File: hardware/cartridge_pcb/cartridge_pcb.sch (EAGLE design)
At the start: 88 parts, among them IC1 LM1117MPX-ADJ, Q1 2N7002, Q2 2N7002, Q3 2N7002, Q4 2N7002, Q5 2N7002, U1 MCP23017-E/SO, U2 ADS1015IDGST, U3 MCP23017-E/SO, U4 TXB0108PWR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

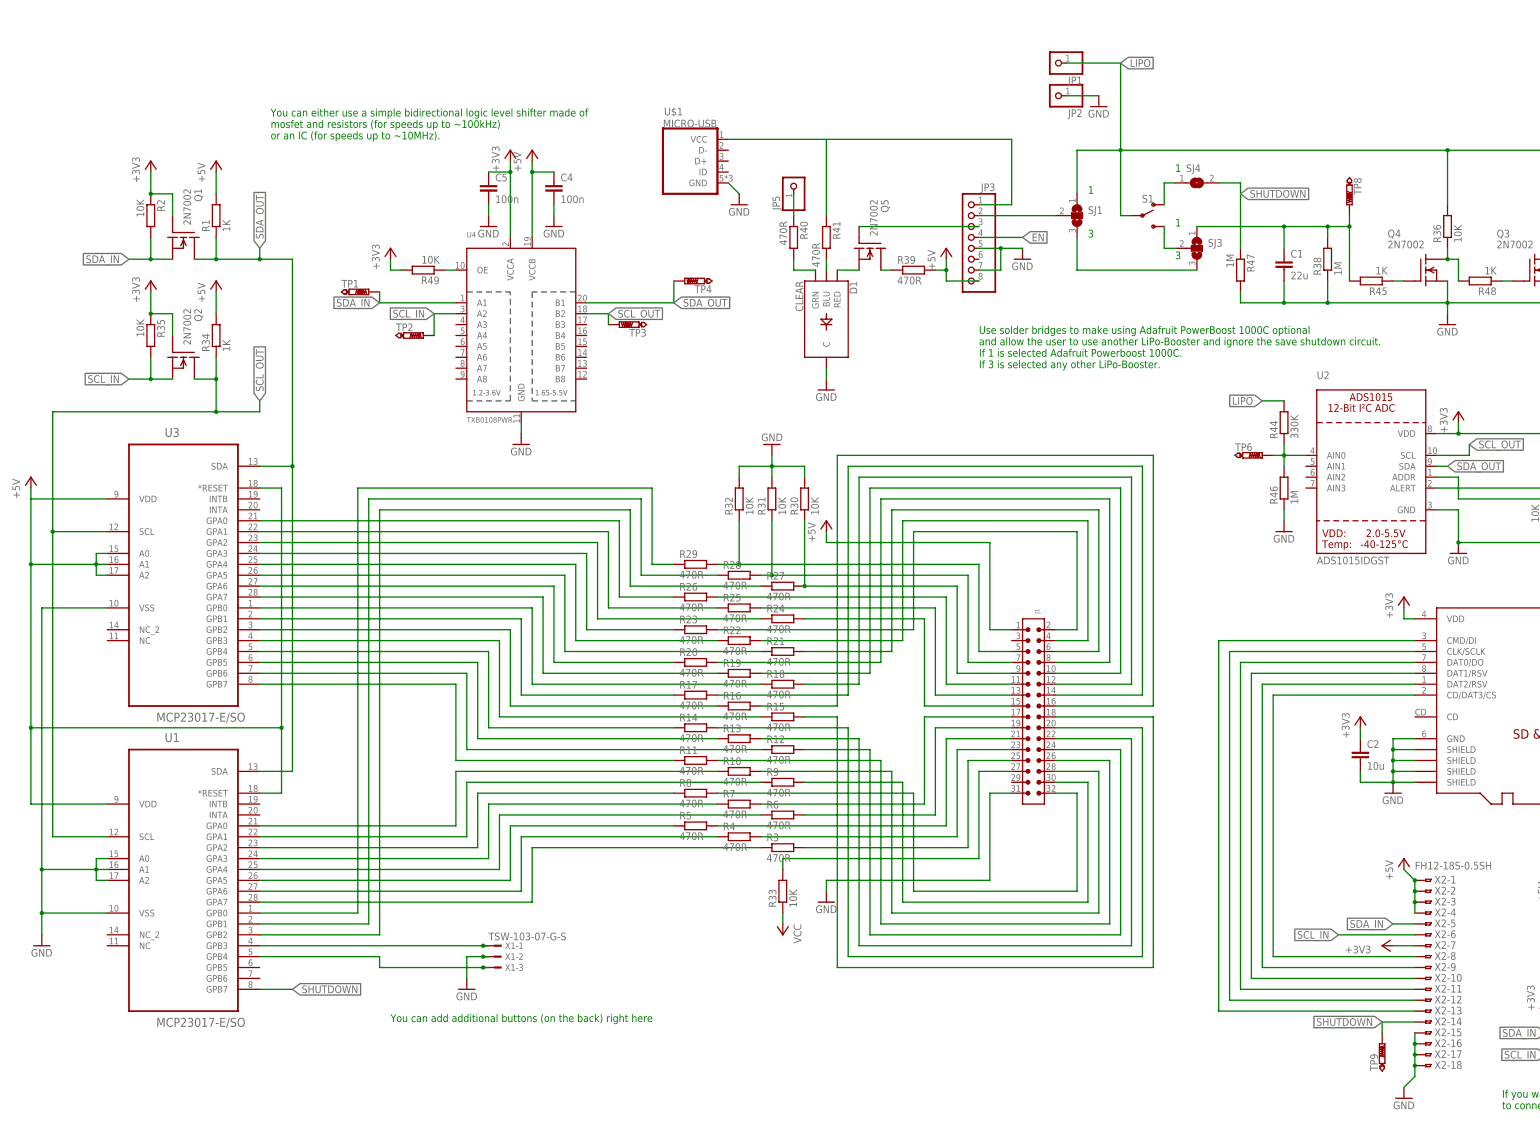
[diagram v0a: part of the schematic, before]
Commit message: fix some issues of the cartridge pcb
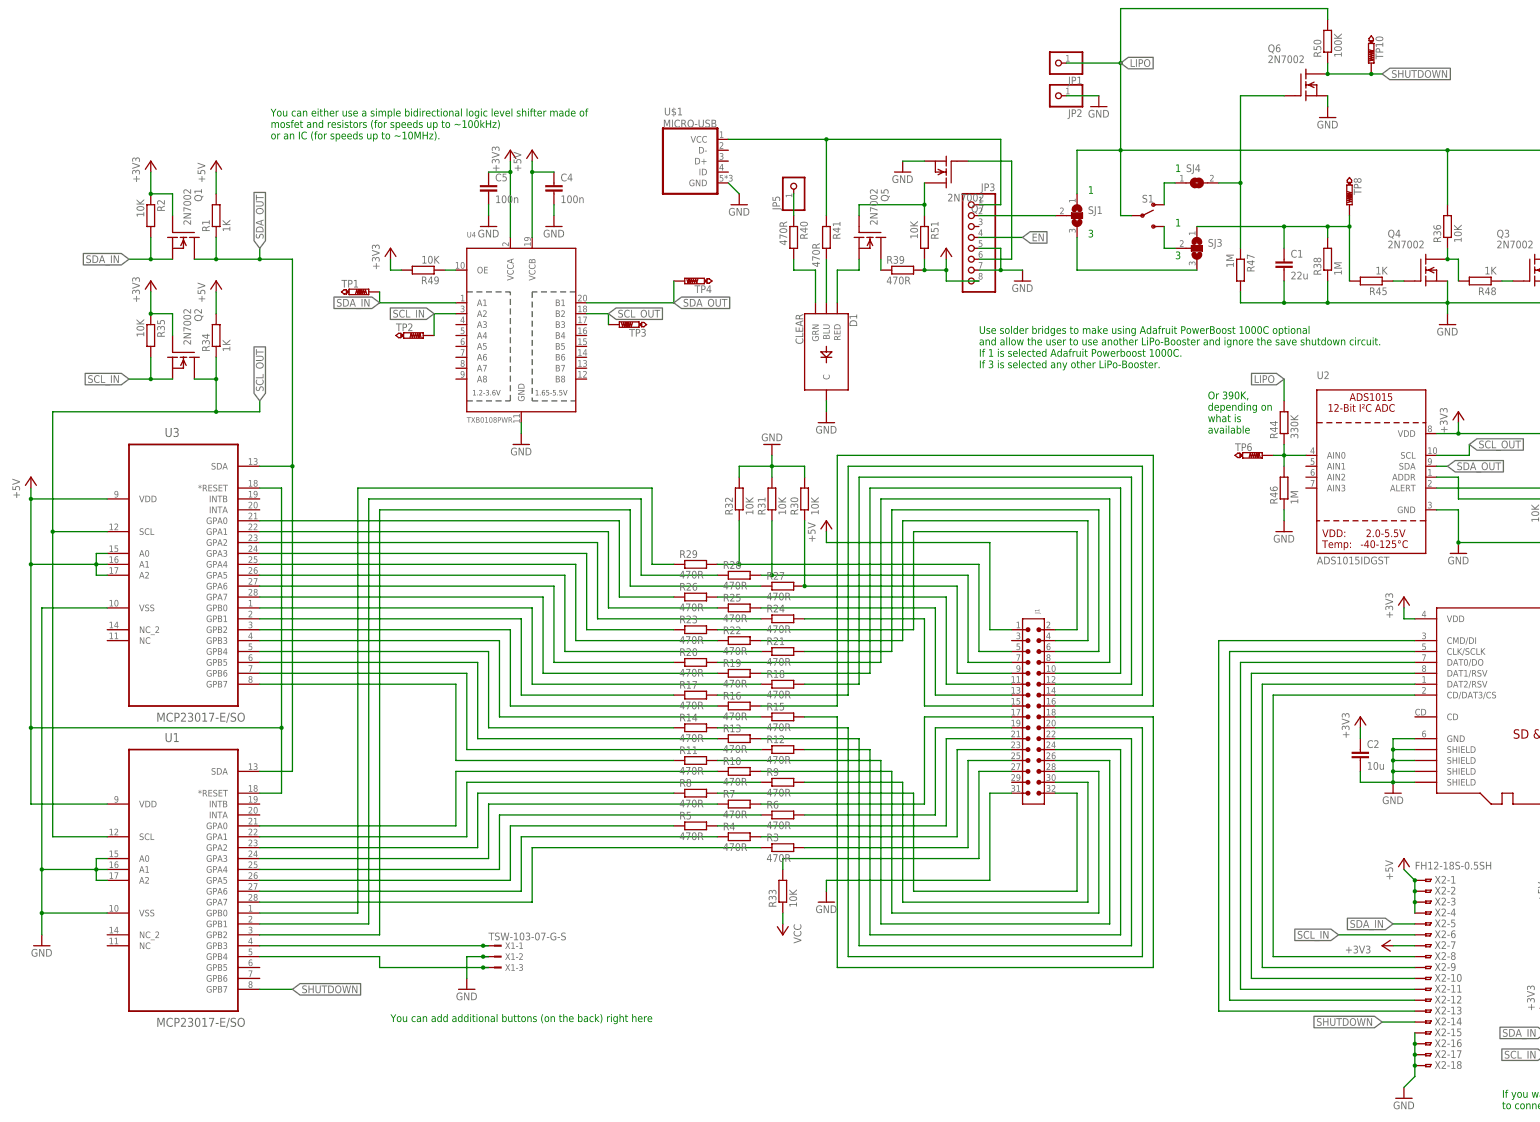
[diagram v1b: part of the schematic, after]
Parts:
- removed TP9: PTR1TP10R, testpad:PTR1TP10R
- added Q6, Q7: 2N7002, transistors_gaui:2N7002
- added R50: 100K, rcl:R-EU_R0805
- added R51: 10K, rcl:R-EU_R0805
- added TP10: PTR1TP10R, testpad:PTR1TP10R
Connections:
- removed net N$29: JP3.1, U$1.VCC
- new net SHUTDOWN_OLD: Q6.G, R47.1, SJ4.2
- net +5V: now also R51.2, U1.*RESET, U1.VDD, U3.*RESET, U3.A0, U3.A1, U3.A2, U3.VDD
- net GND: now also Q6.S, Q7.S
- net LIPO: now also R50.2
- net N$47: now also Q7.D, R51.1; no longer JP3.3
- net N$57: now also JP3.6, Q7.G; no longer U1.*RESET, U1.VDD, U3.*RESET, U3.A0, U3.A1, U3.A2, U3.VDD
- net N$83: now also JP3.1, U$1.VCC
- net SHUTDOWN: now also Q6.D, R50.1, TP10.TP; no longer R47.1, SJ4.2, TP9.TP
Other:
- note added: "Or 390K, depending on what is available"
- moved on the sheet: D1, Q5, R39

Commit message: fix more errors in cartridge pcb which were found while testing the cartridge reader
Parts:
- removed SJ4: (no value), jumper:SJW
- added SJ2: (no value), jumper:SJ2W
- SJ1: device jumper:SJ2WW -> jumper:SJ
- SJ3: device jumper:SJ2WW -> jumper:SJ2W
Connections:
- net LIPO: now also SJ3.1; no longer SJ1.1
- net N$66: now also SJ2.1; no longer SJ3.1
- net N$79: now also SJ2.2; no longer SJ3.2
- net N$80: now also SJ1.1; no longer SJ4.1
- net N$81: now also SJ3.2; no longer SJ1.2
- net N$82: now also SJ2.3; no longer SJ1.3
- net SHUTDOWN_OLD: now also SJ1.2; no longer SJ4.2
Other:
- moved on the sheet: SJ3
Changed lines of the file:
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@@
 <part name="GND11" library="supply1" deviceset="GND" device=""/>
 <part name="R47" library="rcl" library_urn="urn:adsk.eagle:library:334" deviceset="R-EU_" device="R0805" package3d_urn="urn:adsk.eagle:package:23553/2" value="1M"/>
-<part name="SJ1" library="jumper" library_urn="urn:adsk.eagle:library:252" deviceset="SJ2W" device="W" package3d_urn="urn:adsk.eagle:package:15476/1"/>
-<part name="SJ3" library="jumper" library_urn="urn:adsk.eagle:library:252" deviceset="SJ2W" device="W" package3d_urn="urn:adsk.eagle:package:15476/1"/>
 <part name="GND13" library="supply1" deviceset="GND" device=""/>
 <part name="JP5" library="adafruit" deviceset="PINHD-1X1" device=""/>
@@
 <part name="R45" library="rcl" library_urn="urn:adsk.eagle:library:334" deviceset="R-EU_" device="R0805" package3d_urn="urn:adsk.eagle:package:23553/2" value="1K"/>
 <part name="R48" library="rcl" library_urn="urn:adsk.eagle:library:334" deviceset="R-EU_" device="R0805" package3d_urn="urn:adsk.eagle:package:23553/2" value="1K"/>
-<part name="SJ4" library="jumper" library_urn="urn:adsk.eagle:library:252" deviceset="SJ" device="W" package3d_urn="urn:adsk.eagle:package:15507/1"/>
 <part name="U4" library="microbuilder" deviceset="TXB0108PWR" device="" value="TXB0108PWR"/>
 <part name="+3V7" library="supply1" library_urn="urn:adsk.eagle:library:371" deviceset="+3V3" device=""/>
@@
 <part name="R51" library="rcl" library_urn="urn:adsk.eagle:library:334" deviceset="R-EU_" device="R0805" package3d_urn="urn:adsk.eagle:package:23553/2" value="10K"/>
 <part name="GND20" library="supply1" deviceset="GND" device=""/>
+<part name="SJ2" library="jumper" library_urn="urn:adsk.eagle:library:252" deviceset="SJ2W" device="" package3d_urn="urn:adsk.eagle:package:15474/1"/>
+<part name="SJ3" library="jumper" library_urn="urn:adsk.eagle:library:252" deviceset="SJ2W" device="" package3d_urn="urn:adsk.eagle:package:15474/1"/>
+<part name="SJ1" library="jumper" library_urn="urn:adsk.eagle:library:252" deviceset="SJ" device="" package3d_urn="urn:adsk.eagle:package:15471/1"/>
 </parts>
 <sheets>
@@
 <attribute name="VALUE" x="281.178" y="181.61" size="1.778" layer="96" rot="R270"/>
 </instance>
-<instance part="SJ1" gate="G$1" x="246.38" y="190.5" smashed="yes">
-<attribute name="NAME" x="248.92" y="190.881" size="1.778" layer="95"/>
-<attribute name="VALUE" x="248.92" y="188.595" size="1.778" layer="96"/>
-</instance>
-<instance part="SJ3" gate="G$1" x="274.32" y="182.88" smashed="yes">
-<attribute name="NAME" x="276.86" y="183.261" size="1.778" layer="95"/>
-<attribute name="VALUE" x="276.86" y="180.975" size="1.778" layer="96"/>
-</instance>
 <instance part="GND13" gate="1" x="251.46" y="215.9" smashed="yes">
 <attribute name="VALUE" x="248.92" y="213.36" size="1.778" layer="96"/>
@@
 <attribute name="VALUE" x="344.17" y="178.562" size="1.778" layer="96" rot="R180"/>
 </instance>
-<instance part="SJ4" gate="1" x="274.32" y="198.12" smashed="yes">
-<attribute name="NAME" x="271.78" y="200.66" size="1.778" layer="95"/>
-<attribute name="VALUE" x="271.78" y="194.31" size="1.778" layer="96"/>
-</instance>
 <instance part="U4" gate="G$1" x="116.84" y="165.1" smashed="yes">
 <attribute name="NAME" x="104.14" y="185.42" size="1.27" layer="95"/>
@@
 <instance part="GND20" gate="1" x="205.74" y="200.66" smashed="yes">
 <attribute name="VALUE" x="203.2" y="198.12" size="1.778" layer="96"/>
+</instance>
+<instance part="SJ2" gate="G$1" x="274.32" y="182.88" smashed="yes">
+<attribute name="NAME" x="276.86" y="183.261" size="1.778" layer="95"/>
+<attribute name="VALUE" x="276.86" y="180.975" size="1.778" layer="96"/>
+</instance>
+<instance part="SJ3" gate="G$1" x="246.38" y="190.5" smashed="yes">
+<attribute name="NAME" x="248.92" y="190.881" size="1.778" layer="95"/>
+<attribute name="VALUE" x="248.92" y="188.595" size="1.778" layer="96"/>
+</instance>
+<instance part="SJ1" gate="1" x="274.32" y="198.12" smashed="yes">
+<attribute name="NAME" x="271.78" y="200.66" size="1.778" layer="95"/>
+<attribute name="VALUE" x="271.78" y="194.31" size="1.778" layer="96"/>
 </instance>
 </instances>
@@
 <junction x="294.64" y="187.96"/>
 <pinref part="R45" gate="G$1" pin="2"/>
-<pinref part="SJ3" gate="G$1" pin="1"/>
 <wire x1="274.32" y1="187.96" x2="294.64" y2="187.96" width="0.1524" layer="91"/>
 <pinref part="TP8" gate="G$1" pin="TP"/>
 <wire x1="309.88" y1="187.96" x2="309.88" y2="190.5" width="0.1524" layer="91"/>
 <junction x="309.88" y="187.96"/>
+<pinref part="SJ2" gate="G$1" pin="1"/>
 </segment>
 </net>
@@
 <wire x1="358.14" y1="205.74" x2="363.22" y2="205.74" width="0.1524" layer="91"/>
 <wire x1="256.54" y1="205.74" x2="246.38" y2="205.74" width="0.1524" layer="91"/>
-<pinref part="SJ1" gate="G$1" pin="1"/>
 <wire x1="246.38" y1="205.74" x2="246.38" y2="195.58" width="0.1524" layer="91"/>
 <wire x1="256.54" y1="226.06" x2="256.54" y2="238.76" width="0.1524" layer="91"/>
@@
 <wire x1="304.8" y1="236.22" x2="304.8" y2="238.76" width="0.1524" layer="91"/>
 <wire x1="256.54" y1="238.76" x2="304.8" y2="238.76" width="0.1524" layer="91"/>
+<pinref part="SJ3" gate="G$1" pin="1"/>
 </segment>
 <segment>
@@
 <pinref part="S1" gate="1" pin="S"/>
 <wire x1="266.7" y1="187.96" x2="266.7" y2="182.88" width="0.1524" layer="91"/>
-<pinref part="SJ3" gate="G$1" pin="2"/>
 <wire x1="266.7" y1="182.88" x2="269.24" y2="182.88" width="0.1524" layer="91"/>
+<pinref part="SJ2" gate="G$1" pin="2"/>
 </segment>
 </net>
@@
 <wire x1="266.7" y1="193.04" x2="266.7" y2="198.12" width="0.1524" layer="91"/>
 <wire x1="266.7" y1="198.12" x2="269.24" y2="198.12" width="0.1524" layer="91"/>
-<pinref part="SJ4" gate="1" pin="1"/>
+<pinref part="SJ1" gate="1" pin="1"/>
 </segment>
 </net>
@@
 <segment>
 <pinref part="JP3" gate="A" pin="2"/>
-<pinref part="SJ1" gate="G$1" pin="2"/>
 <wire x1="223.52" y1="190.5" x2="241.3" y2="190.5" width="0.1524" layer="91"/>
+<pinref part="SJ3" gate="G$1" pin="2"/>
 </segment>
 </net>
 <net name="N$82" class="0">
 <segment>
-<pinref part="SJ1" gate="G$1" pin="3"/>
 <wire x1="246.38" y1="185.42" x2="246.38" y2="177.8" width="0.1524" layer="91"/>
+<wire x1="246.38" y1="177.8" x2="274.32" y2="177.8" width="0.1524" layer="91"/>
+<pinref part="SJ2" gate="G$1" pin="3"/>
 <pinref part="SJ3" gate="G$1" pin="3"/>
-<wire x1="246.38" y1="177.8" x2="274.32" y2="177.8" width="0.1524" layer="91"/>
 </segment>
 </net>
@@
 <segment>
 <pinref part="R47" gate="G$1" pin="1"/>
-<pinref part="SJ4" gate="1" pin="2"/>
 <wire x1="284.48" y1="198.12" x2="284.48" y2="182.88" width="0.1524" layer="91"/>
 <wire x1="279.4" y1="198.12" x2="284.48" y2="198.12" width="0.1524" layer="91"/>
@@
 <wire x1="284.48" y1="218.44" x2="294.64" y2="218.44" width="0.1524" layer="91"/>
 <pinref part="Q6" gate="G$1" pin="G"/>
-</segment>
-</net>
+<pinref part="SJ1" gate="1" pin="2"/>
+</segment>
+</net>

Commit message: fixed error in cpcb
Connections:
- removed net VCC: R33.1
- net +5V: now also R33.1
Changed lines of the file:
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@@
 <part name="GND3" library="supply1" deviceset="GND" device=""/>
 <part name="R33" library="rcl" library_urn="urn:adsk.eagle:library:334" deviceset="R-EU_" device="R0805" package3d_urn="urn:adsk.eagle:package:23553/2" value="10K"/>
-<part name="P+3" library="supply1" deviceset="VCC" device=""/>
 <part name="Q1" library="transistors_gaui" deviceset="2N7002" device=""/>
 <part name="R1" library="rcl" library_urn="urn:adsk.eagle:library:334" deviceset="R-EU_" device="R0805" package3d_urn="urn:adsk.eagle:package:23553/2" value="1K"/>
@@
 <part name="SJ3" library="jumper" library_urn="urn:adsk.eagle:library:252" deviceset="SJ2W" device="" package3d_urn="urn:adsk.eagle:package:15474/1"/>
 <part name="SJ1" library="jumper" library_urn="urn:adsk.eagle:library:252" deviceset="SJ" device="" package3d_urn="urn:adsk.eagle:package:15471/1"/>
+<part name="P+3" library="supply1" library_urn="urn:adsk.eagle:library:371" deviceset="+5V" device=""/>
 </parts>
 <sheets>
@@
 <attribute name="VALUE" x="181.102" y="29.21" size="1.778" layer="96" rot="R90"/>
 </instance>
-<instance part="P+3" gate="VCC" x="177.8" y="22.86" smashed="yes" rot="R180">
-<attribute name="VALUE" x="180.34" y="25.4" size="1.778" layer="96" rot="R270"/>
-</instance>
 <instance part="Q1" gate="G$1" x="38.1" y="185.42" smashed="yes" rot="R270">
 <attribute name="VALUE" x="38.1" y="196.85" size="1.778" layer="96" rot="R270"/>
@@
 <attribute name="NAME" x="271.78" y="200.66" size="1.778" layer="95"/>
 <attribute name="VALUE" x="271.78" y="194.31" size="1.778" layer="96"/>
+</instance>
+<instance part="P+3" gate="1" x="172.72" y="27.94" smashed="yes">
+<attribute name="VALUE" x="170.18" y="22.86" size="1.778" layer="96" rot="R90"/>
 </instance>
 </instances>
@@
 <pinref part="Q7" gate="G$1" pin="S"/>
 <wire x1="205.74" y1="203.2" x2="210.82" y2="203.2" width="0.1524" layer="91"/>
-</segment>
-</net>
-<net name="VCC" class="0">
-<segment>
-<pinref part="R33" gate="G$1" pin="1"/>
-<pinref part="P+3" gate="VCC" pin="VCC"/>
-<wire x1="177.8" y1="27.94" x2="177.8" y2="25.4" width="0.1524" layer="91"/>
 </segment>
 </net>
@@
 <junction x="2.54" y="109.22"/>
 </segment>
-</net>
+<segment>
+<pinref part="R33" gate="G$1" pin="1"/>
+<wire x1="177.8" y1="27.94" x2="177.8" y2="25.4" width="0.1524" layer="91"/>
+<pinref part="P+3" gate="1" pin="+5V"/>
+<wire x1="177.8" y1="25.4" x2="172.72" y2="25.4" width="0.1524" layer="91"/>
+</segment>
+</net>
